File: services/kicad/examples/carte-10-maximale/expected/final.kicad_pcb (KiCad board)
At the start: 2 copper layers, 140 x 105 mm, 70 parts, among them J1 IN_5V, J2 SWD, J3 IO0, J4 IO1, J5 IO2, J6 IO3, J7 IO4, U1 STM32F103C8T6, U2 AMS1117-3.3

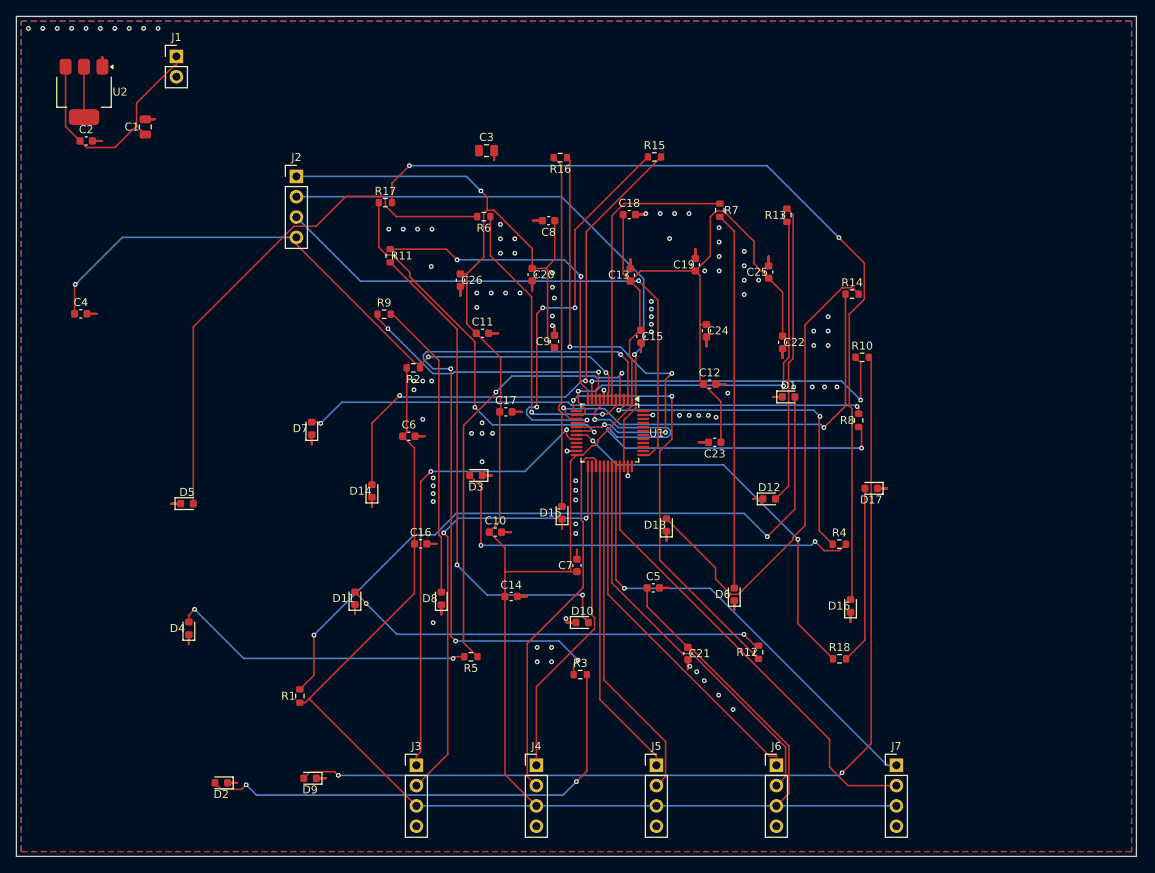
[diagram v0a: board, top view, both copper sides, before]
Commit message: feat(kicad): placement pro et routage 100 % fabricable sur les 16 cartes -- integration sur main (#164)
Branche d'integration coupee depuis origin/main (fab2a82, PR #162) : les
fichiers cles de main etaient des instantanes de feat/placement-seed-snap-
bypass (routing.py = 7981019, placement.py = 437a8b4...). On reprend donc
l'arbre entier de cette branche (345 commits, dernier 9f48667) et on y
conserve ce que main seul apportait :
- tools/verrou_routage.py + son test : « 6,2 Go par routage » rectifie
  (0,2 Go mesure ; c'est la concurrence qui emballe la memoire) ;
- tests/test_driver_llm_resync.py ;
- CLAUDE.md, PLAN.md, DECISIONS.md : fusion a trois voies, les sections
  des deux lignes conservees (2026-09-05 conteneur/verrou, 2026-09-07
  parcours asynchrone et chaine du driver, 2026-09-09/10 lecons).
Les skills *-delegate restent supprimes (remplaces le 2026-08-30).

Contenu : banc en deux phases (placement valide puis routage gele), snap
sur les regles natives, repli GND cible, journal Freerouting incremental,
horloge sans progres, via d'echappement vers le plan principal,
serigraphie degagee ; 16 cartes livrees a 100 %, 0 erreur DRC.

Verification : pytest services/kicad 1805 passed, 16 skipped ;
pnpm type-check 8/8.


Claude-Session: https://claude.ai/code/session_01TnMqm4La2CxQHHB5K8aSSV

Co-authored-by: Claude Fable 5.1 <noreply@anthropic.com>
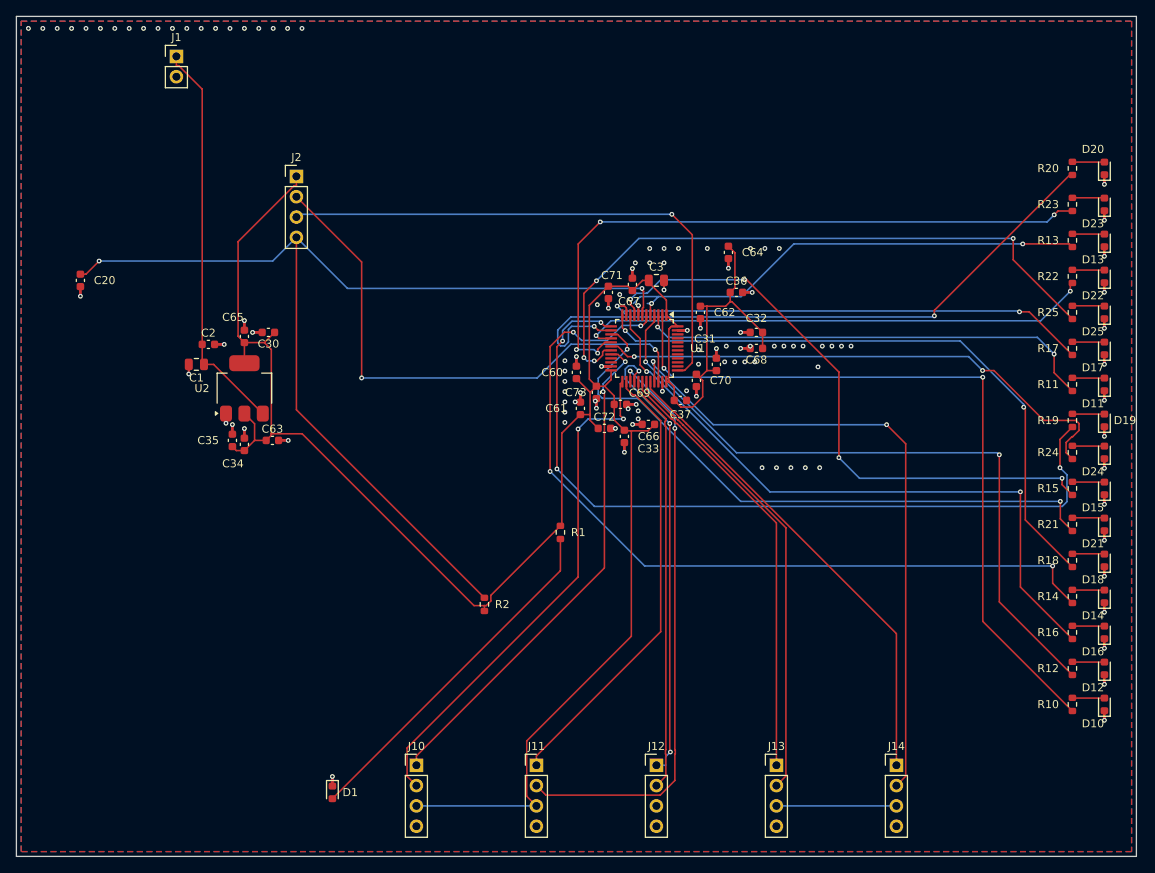
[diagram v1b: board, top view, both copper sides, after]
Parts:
- removed C10, C11, C12, C13, C14, C15, C16, C17, C18, C19, C21, C22, C23, C24, C25, C26, C4, C5, C6, C7, C8, C9: 100nF, C_0603_1608Metric
- removed D2, D3, D4, D5, D6, D7, D8, D9: LED, LED_0603_1608Metric
- removed J3: IO0, PinHeader_1x04_P2.54mm_Vertical
- removed J4: IO1, PinHeader_1x04_P2.54mm_Vertical
- removed J5: IO2, PinHeader_1x04_P2.54mm_Vertical
- removed J6: IO3, PinHeader_1x04_P2.54mm_Vertical
- removed J7: IO4, PinHeader_1x04_P2.54mm_Vertical
- removed R3, R4, R5, R6, R7, R8, R9: 1k, R_0603_1608Metric
- added C30: 100nF, C_0603_1608Metric, F.Cu at (110.0, 92.0)
- added C31: 100nF, C_0603_1608Metric, F.Cu at (166.0, 96.0)
- added C32: 100nF, C_0603_1608Metric, F.Cu at (171.0, 92.0)
- added C33: 100nF, C_0603_1608Metric, F.Cu at (157.5, 103.5)
- added C34: 100nF, C_0603_1608Metric, F.Cu at (107.0, 106.0)
- added C35: 100nF, C_0603_1608Metric, F.Cu at (105.5, 105.5)
- added C36: 100nF, C_0603_1608Metric, F.Cu at (168.5, 87.0)
- added C37: 100nF, C_0603_1608Metric, F.Cu at (161.5, 100.5)
- added C60: 100nF, C_0603_1608Metric, F.Cu at (148.5, 97.0)
- added C61: 100nF, C_0603_1608Metric, F.Cu at (149.0, 101.5)
- added C62: 100nF, C_0603_1608Metric, F.Cu at (164.0, 89.5)
- added C63: 100nF, C_0603_1608Metric, F.Cu at (110.5, 105.5)
- added C64: 100nF, C_0603_1608Metric, F.Cu at (167.5, 82.0)
- added C65: 100nF, C_0603_1608Metric, F.Cu at (107.0, 92.5)
- added C66: 100nF, C_0603_1608Metric, F.Cu at (154.5, 105.0)
- added C67: 100nF, C_0603_1608Metric, F.Cu at (152.5, 87.0)
- added C68: 100nF, C_0603_1608Metric, F.Cu at (171.0, 94.0)
- added C69: 100nF, C_0603_1608Metric, F.Cu at (154.0, 101.0)
- added C70: 100nF, C_0603_1608Metric, F.Cu at (163.5, 98.0)
- added C71: 100nF, C_0603_1608Metric, F.Cu at (155.5, 86.0)
- added C72: 100nF, C_0603_1608Metric, F.Cu at (152.0, 104.0)
- added C73: 100nF, C_0603_1608Metric, F.Cu at (151.0, 99.5)
- added D18: LED, LED_0603_1608Metric, F.Cu at (214.5, 120.5)
- added D19: LED, LED_0603_1608Metric, F.Cu at (214.5, 103.0)
- added D20: LED, LED_0603_1608Metric, F.Cu at (214.5, 71.5)
- added D21: LED, LED_0603_1608Metric, F.Cu at (214.5, 116.0)
- added D22: LED, LED_0603_1608Metric, F.Cu at (214.5, 85.0)
- added D23: LED, LED_0603_1608Metric, F.Cu at (214.5, 76.0)
- added D24: LED, LED_0603_1608Metric, F.Cu at (214.5, 107.0)
- added D25: LED, LED_0603_1608Metric, F.Cu at (214.5, 89.5)
- added J10: IO0, PinHeader_1x04_P2.54mm_Vertical, F.Cu at (128.5, 146.1)
- added J11: IO1, PinHeader_1x04_P2.54mm_Vertical, F.Cu at (143.5, 146.1)
- added J12: IO2, PinHeader_1x04_P2.54mm_Vertical, F.Cu at (158.5, 146.1)
- added J13: IO3, PinHeader_1x04_P2.54mm_Vertical, F.Cu at (173.5, 146.1)
- added J14: IO4, PinHeader_1x04_P2.54mm_Vertical, F.Cu at (188.5, 146.1)
- added R19: 1k, R_0603_1608Metric, F.Cu at (210.5, 103.0)
- added R20: 1k, R_0603_1608Metric, F.Cu at (210.5, 71.5)
- added R21: 1k, R_0603_1608Metric, F.Cu at (210.5, 116.0)
- added R22: 1k, R_0603_1608Metric, F.Cu at (210.5, 85.0)
- added R23: 1k, R_0603_1608Metric, F.Cu at (210.5, 76.0)
- added R24: 1k, R_0603_1608Metric, F.Cu at (210.5, 107.0)
- added R25: 1k, R_0603_1608Metric, F.Cu at (210.5, 89.5)
- moved D11 97.4 mm to (214.5, 98.5)
- moved D14 92.5 mm to (214.5, 125.0)
- moved R17 87.8 mm to (210.5, 94.0), turned to 90 degrees
- moved R16 87.3 mm to (210.5, 129.5), turned to 90 degrees
- moved R11 86.8 mm to (210.5, 98.5), turned to 90 degrees
- moved D1 75.5 mm to (118.0, 149.5), turned to -90 degrees
- moved D15 67.9 mm to (214.5, 111.5)
- moved R15 66.7 mm to (210.5, 111.5), turned to 90 degrees
- moved D10 66.1 mm to (214.5, 138.5), turned to 90 degrees
- moved D13 65.3 mm to (214.5, 80.5)
- moved C20 56.5 mm to (86.5, 85.5)
- moved R10 50.7 mm to (210.5, 138.5), turned to 90 degrees
- moved D12 47.0 mm to (214.5, 134.0), turned to 90 degrees
- moved R14 46.8 mm to (210.5, 125.0), turned to 90 degrees
- moved U2 42.1 mm to (107.0, 99.0), turned to 90 degrees
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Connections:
- C20 pad 1: +3V3 -> NRST
- C3 pad 1: Net-(C3-1) -> +3V3
- D10 pad 2: LEDA8 -> LEDA0
- D11 pad 2: LEDA9 -> LEDA1
- D12 pad 2: LEDA10 -> LEDA2
- D13 pad 2: LEDA11 -> LEDA3
- D14 pad 2: LEDA12 -> LEDA4
- D15 pad 2: LEDA13 -> LEDA5
- D16 pad 2: LEDA14 -> LEDA6
- D17 pad 2: LEDA15 -> LEDA7
- R10 pad 1: IO_L7 -> IO_L0
- R10 pad 2: LEDA7 -> LEDA0
- R11 pad 1: IO_L8 -> IO_L1
- R11 pad 2: LEDA8 -> LEDA1
- R12 pad 1: IO_L9 -> IO_L2
- R12 pad 2: LEDA9 -> LEDA2
- R13 pad 1: IO_L10 -> IO_L3
- R13 pad 2: LEDA10 -> LEDA3
- R14 pad 1: IO_L11 -> IO_L4
- R14 pad 2: LEDA11 -> LEDA4
- R15 pad 1: IO_L12 -> IO_L5
- R15 pad 2: LEDA12 -> LEDA5
- R16 pad 1: IO_L13 -> IO_L6
- R16 pad 2: LEDA13 -> LEDA6
- R17 pad 1: IO_L14 -> IO_L7
- R17 pad 2: LEDA14 -> LEDA7
- R18 pad 1: IO_L15 -> IO_L8
- R18 pad 2: LEDA15 -> LEDA8
- U1 pad 36: Net-(U1-36) -> +3V3
- U1 pad 48: Net-(U1-48) -> +3V3
- U2 pad 2: Net-(U2-2) -> +3V3
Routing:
- net LEDA7: track 121.5 -> 4.02 mm, vias 2 -> 0
- net LEDA14: track 110.5 -> 4.02 mm, vias 2 -> 0
- net +3V3: track 419.2 -> 329.4 mm, vias 1 -> 0
- net IO_L4: track 37.1 -> 104.0 mm, vias 0 -> 4
- net LEDA5: track 70.5 -> 4.02 mm, vias 2 -> 0
- net LEDA12: track 68.6 -> 4.02 mm, vias 2 -> 0
- net LEDA3: track 65.8 -> 4.02 mm
- net GND: track 172.8 -> 114.0 mm, vias 99 -> 114
- net LEDA8: track 62.3 -> 4.02 mm, vias 2 -> 0
- net LEDA0: track 60.9 -> 4.02 mm, vias 2 -> 0
- net LEDA11: track 59.8 -> 4.02 mm
- net LEDA1: track 55.9 -> 4.02 mm, vias 2 -> 0
- net LEDA9: track 53.2 -> 4.02 mm, vias 2 -> 0
- net NRST: track 84.8 -> 133.0 mm, vias 3 -> 2
- net IO_L9: track 52.6 -> 100.7 mm, vias 2 -> 4
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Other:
- copper layers 2 -> 4

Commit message: chore(banc): relivrer carte-01..10 avec la couture corrigee
Boards reroutes par HTTP depuis placement.kicad_pcb inchange, avec le
code de #217. Juges par remesurer_banc.py : 0 erreur, 0 connexion
manquante sur les dix. 678 -> 443 vias ; la rangee de vias GND du bord
haut a disparu.

mesures.json : `board` recompte, `drc_du_board` rejuge, nouvelle cle
`couture_corrigee` (date, vias_avant, couches). journal.txt et les
champs du run d origine sont laisses tels quels et le disent.
rendu-3d.png : kicad-cli, modeles 3D, iso 1400x900.

Couches d un tirage : huit cartes sur 2, carte-08 et carte-10 sur 4.
CLAUDE.md et BANC_DRIVER_LLM.md recomptes. carte-11 non touchee.

Co-Authored-By: Claude Opus 5 (1M context) <noreply@anthropic.com>
Claude-Session: https://claude.ai/code/session_01TnMqm4La2CxQHHB5K8aSSV
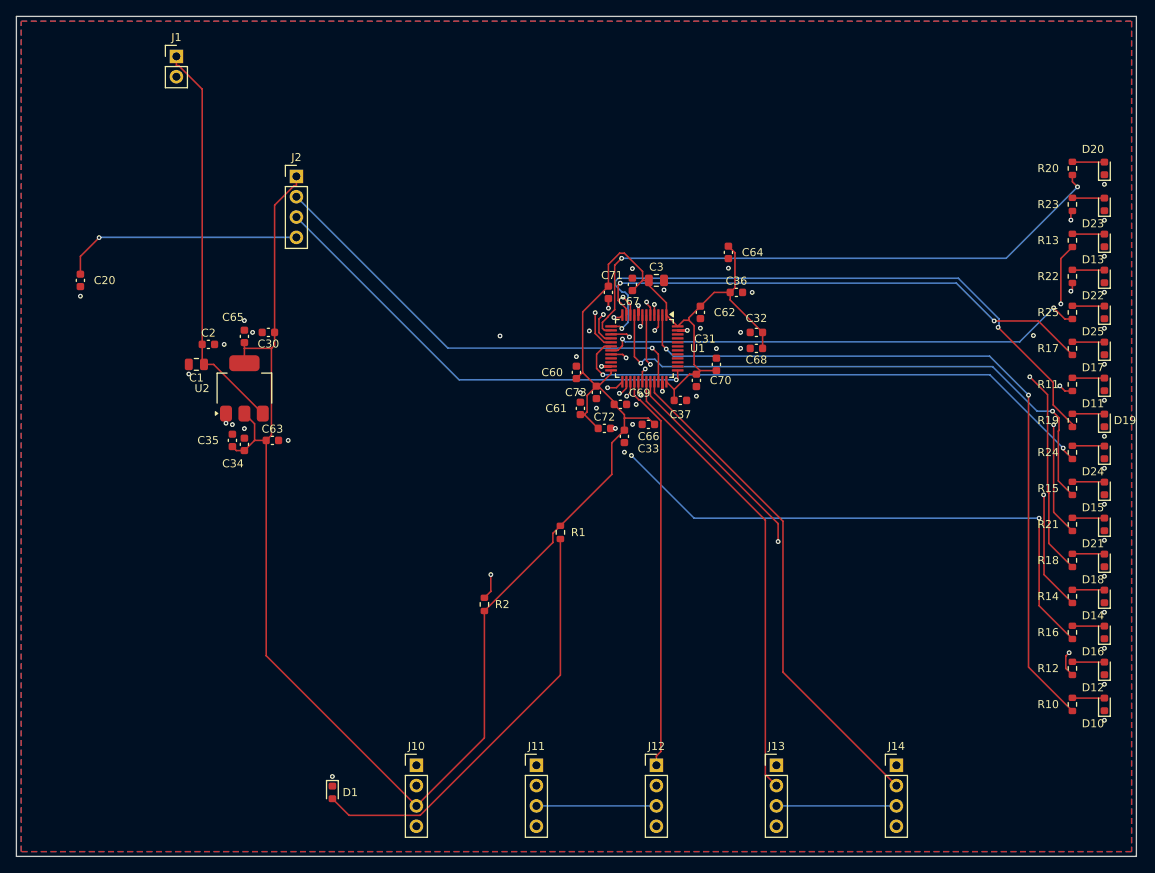
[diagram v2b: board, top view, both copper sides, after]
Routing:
- net GND: track 114.0 -> 15.6 mm, vias 114 -> 48
- net IO_L4: track 104.0 -> 77.3 mm, vias 4 -> 2
- net IO_L9: track 100.7 -> 76.2 mm, vias 4 -> 2
- net IO_L15: track 82.0 -> 61.2 mm, vias 4 -> 2
- net NRST: track 133.0 -> 114.2 mm, vias 2 -> 4
- net EXT4_2: track 81.9 -> 63.0 mm, vias 2 -> 0
- net EXT1_2: track 73.4 -> 55.4 mm, vias 2 -> 1
- net +3V3: track 329.4 -> 316.2 mm
- net IO_L6: track 81.9 -> 94.9 mm, vias 2 -> 3
- net SWDIO: track 68.9 -> 56.8 mm, vias 2 -> 1
- net SWCLK: track 68.9 -> 57.2 mm
- net IO_L13: track 82.1 -> 71.5 mm, vias 4 -> 2
- net IO_L10: track 83.4 -> 73.4 mm
- net LED_PWR: track 44.3 -> 53.6 mm
- net IO_L2: track 86.6 -> 95.1 mm, vias 2 -> 3
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
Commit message: chore(banc): banc en deux phases (placement valide, puis routage gele) ; relivrer carte-10 compacte (#228)
Consigne de l utilisateur : placement d abord, routage ensuite, pas
d aller-retour. Code de #226 et #227, un tirage par carte, par HTTP.

Phase A : dix placements sur dix valides — 0 erreur DRC sur le board place,
connecteur le plus loin d un bord a 2,0 mm.
Phase B : placements GELES routes. 0 erreur DRC sur les dix ; 01-05 et 10 a
0 connexion manquante ; 06:1, 07:2, 08:8, 09:11.

carte-10 relivree : 140 x 105 -> 60,9 x 45,7, 6 couches, 0 erreur,
0 manquante ; mesures.json rejuge par remesurer_banc.py, rendu refait.

08 et 09 : le board livre est celui du palier 2 couches ; les paliers 4 et 6
couches allaient plus loin (jusqu a ~96 %) puis figeaient sans rendre de
board. Tableau et journal dans BANC_DRIVER_LLM.md.


Claude-Session: https://claude.ai/code/session_01TnMqm4La2CxQHHB5K8aSSV

Co-authored-by: Claude Fable 5.1 <noreply@anthropic.com>
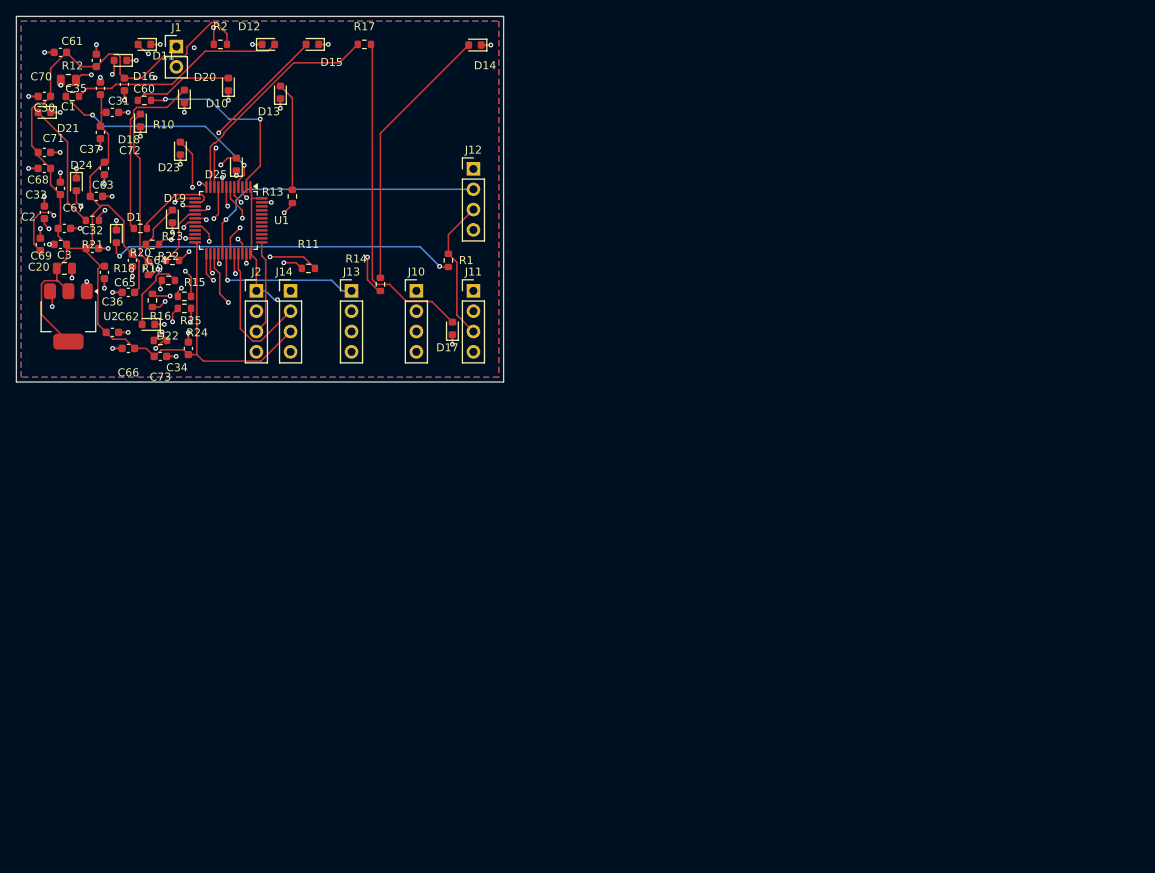
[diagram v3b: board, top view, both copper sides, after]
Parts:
- moved R12 144.0 mm to (85.5, 62.5), turned to 0 degrees
- moved D16 142.3 mm to (91.5, 58.0), turned to 180 degrees
- moved D21 142.2 mm to (82.0, 64.5), turned to 180 degrees
- moved R10 138.4 mm to (94.5, 63.0), turned to 180 degrees
- moved D10 134.2 mm to (105.0, 61.0)
- moved D24 132.8 mm to (86.0, 73.5), turned to -90 degrees
- moved D18 132.5 mm to (94.0, 65.5)
- moved D12 130.4 mm to (110.0, 56.0), turned to 0 degrees
- moved R21 128.3 mm to (88.0, 78.0), turned to 180 degrees
- moved D11 127.3 mm to (94.5, 56.0), turned to 180 degrees
- moved R18 121.1 mm to (95.0, 84.0)
- moved R16 119.7 mm to (96.5, 93.0), turned to 0 degrees
- moved D22 119.7 mm to (95.0, 91.0), turned to 180 degrees
- moved D19 119.3 mm to (98.0, 77.5)
- moved R15 117.4 mm to (95.5, 88.0), turned to -90 degrees
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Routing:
- net +3V3: track 316.2 -> 231.6 mm, vias 0 -> 1
- net IO_L0: track 93.9 -> 24.0 mm
- net IO_L8: track 82.2 -> 15.4 mm
- net IO_L2: track 95.1 -> 28.9 mm, vias 3 -> 2
- net IO_L9: track 76.2 -> 10.3 mm
- net IO_L13: track 71.5 -> 7.73 mm, vias 2 -> 0
- net IO_L10: track 73.4 -> 11.0 mm, vias 2 -> 0
- net IO_L6: track 94.9 -> 33.2 mm, vias 3 -> 2
- net IO_L11: track 74.4 -> 13.2 mm
- net IO_L5: track 72.3 -> 18.5 mm
- net IO_L3: track 61.7 -> 9.81 mm
- net IO_L14: track 68.3 -> 17.4 mm
- net EXT4_1: track 60.7 -> 10.3 mm
- net IO_L15: track 61.2 -> 11.1 mm
- net IO_L12: track 65.8 -> 15.7 mm
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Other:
- board size 140 x 105 mm -> 60.9 x 45.7 mm
- copper layers 4 -> 6
